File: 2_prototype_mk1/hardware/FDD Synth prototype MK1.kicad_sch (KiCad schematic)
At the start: 4 parts, among them U1 74AHCT245d

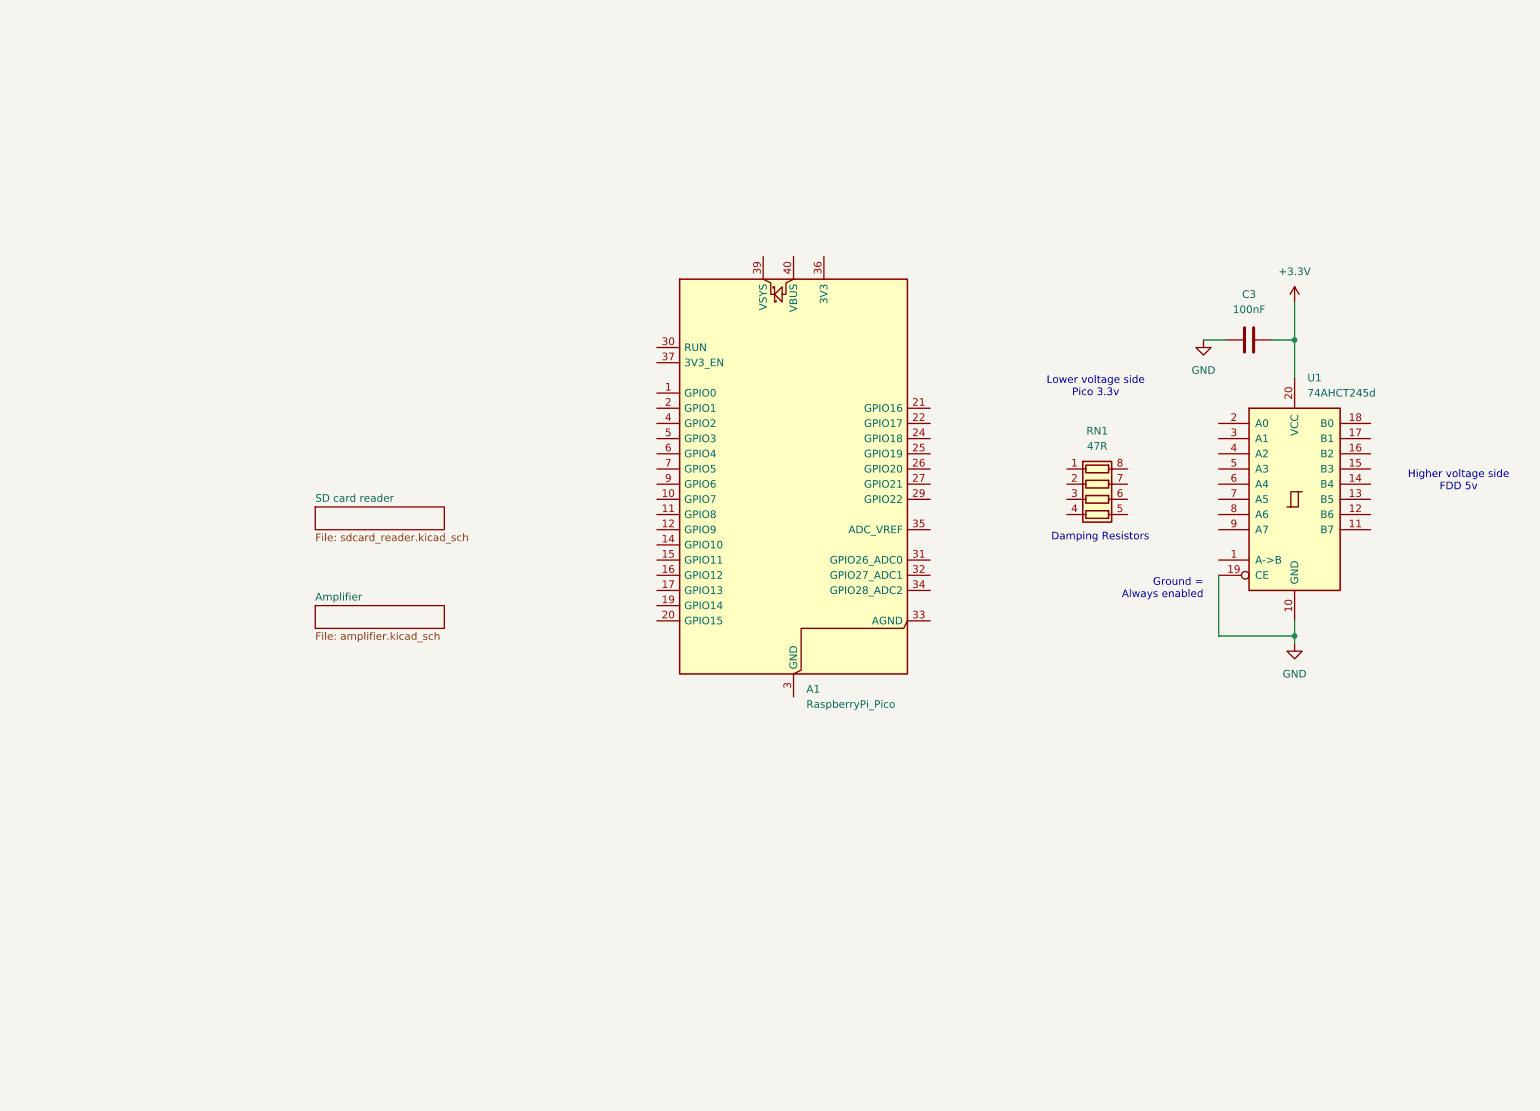
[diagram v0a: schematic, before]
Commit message: Created basic PCB
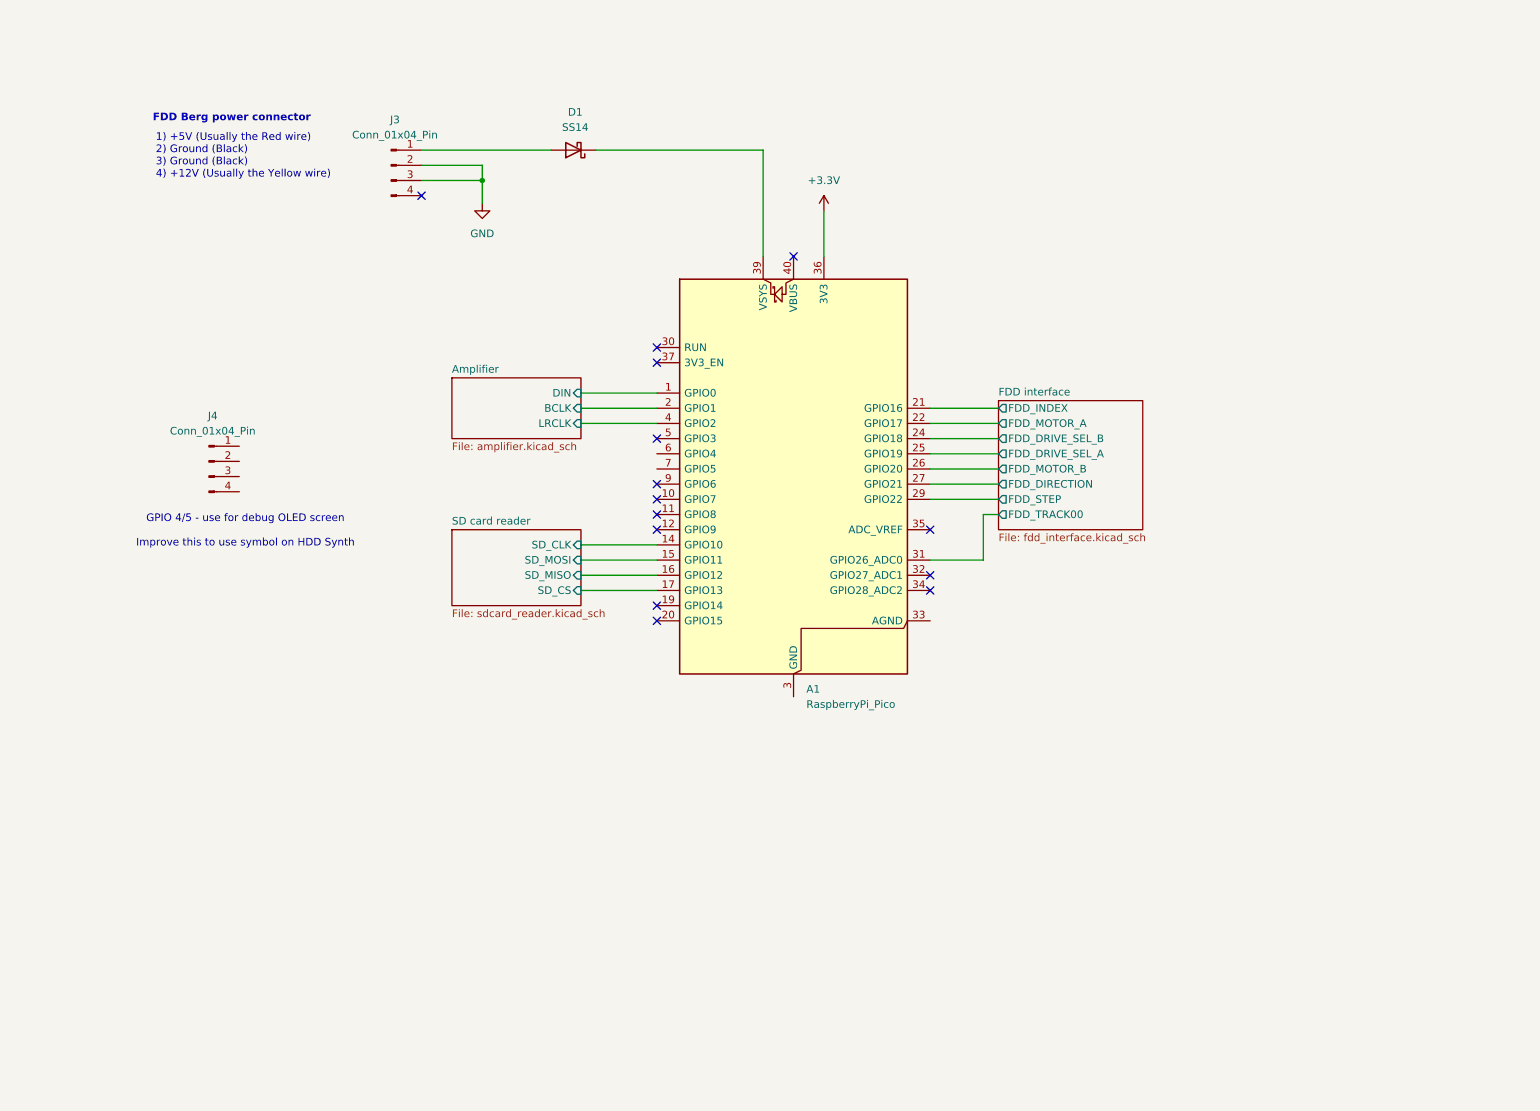
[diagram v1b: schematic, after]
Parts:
- removed C3: 100nF, Capacitor_SMD:C_0603_1608Metric, symbol Device:C
- removed RN1: 47R, Resistor_SMD:R_Array_Convex_4x0603, symbol Device:R_Pack04
- removed U1: 74AHCT245d, Package_SO:SOIC-20W_7.5x12.8mm_P1.27mm, symbol 74xx:74LS245
- added D1: SS14, Diode_SMD:D_SMA, symbol Device:D_Schottky
- added J3: Conn_01x04_Pin, Connector_JST:JST_XH_B4B-XH-A_1x04_P2.50mm_Vertical, symbol Connector:Conn_01x04_Pin
- added J4: Conn_01x04_Pin, Connector_PinSocket_2.54mm:PinSocket_1x04_P2.54mm_Vertical, symbol Connector:Conn_01x04_Pin
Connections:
- net +3.3V: now also A1.36 (3V3)
- net GND: now also J3.2 (Pin_2), J3.3 (Pin_3)
- net Amplifier/DIN: now reaches A1.1 (GPIO0)
- net SD card reader/SD_CLK: now reaches A1.14 (GPIO10)
- net SD card reader/SD_MOSI: now reaches A1.15 (GPIO11)
- net SD card reader/SD_MISO: now reaches A1.16 (GPIO12)
- net SD card reader/SD_CS: now reaches A1.17 (GPIO13)
- net Amplifier/BCLK: now reaches A1.2 (GPIO1)
- net FDD interface/FDD_INDEX: now reaches A1.21 (GPIO16)
- net FDD interface/FDD_MOTOR_A: now reaches A1.22 (GPIO17)
- net FDD interface/FDD_DRIVE_SEL_B: now reaches A1.24 (GPIO18)
- net FDD interface/FDD_DRIVE_SEL_A: now reaches A1.25 (GPIO19)
- net FDD interface/FDD_MOTOR_B: now reaches A1.26 (GPIO20)
- net FDD interface/FDD_DIRECTION: now reaches A1.27 (GPIO21)
- net FDD interface/FDD_STEP: now reaches A1.29 (GPIO22)
- net FDD interface/FDD_TRACK00: now reaches A1.31 (GPIO26_ADC0)
- net at A1.39 (VSYS): now also D1.1 (K)
- net Amplifier/LRCLK: now reaches A1.4 (GPIO2)
- new net: D1.2 (A), J3.1 (Pin_1)
- no-connect marks 0 -> 14
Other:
- added sheet FDD interface (fdd_interface.kicad_sch)
- sheet Amplifier ports: added BCLK, DIN, LRCLK; removed none
- sheet SD card reader ports: added SD_CLK, SD_CS, SD_MISO, SD_MOSI; removed none
- note added: "1) +5V (Usually the Red wire) 2) Ground (Black) 3) Ground (Black) 4) +12V (Usually the Yellow wire)"
- note added: "FDD Berg power connector"
- note added: "GPIO 4/5 - use for debug OLED screen Improve this to use symbol on HDD Synth"
- note removed: "Damping Resistors"
- note removed: "Ground = Always enabled"
- note removed: "Higher voltage side FDD 5v"
- note removed: "Lower voltage side Pico 3.3v"

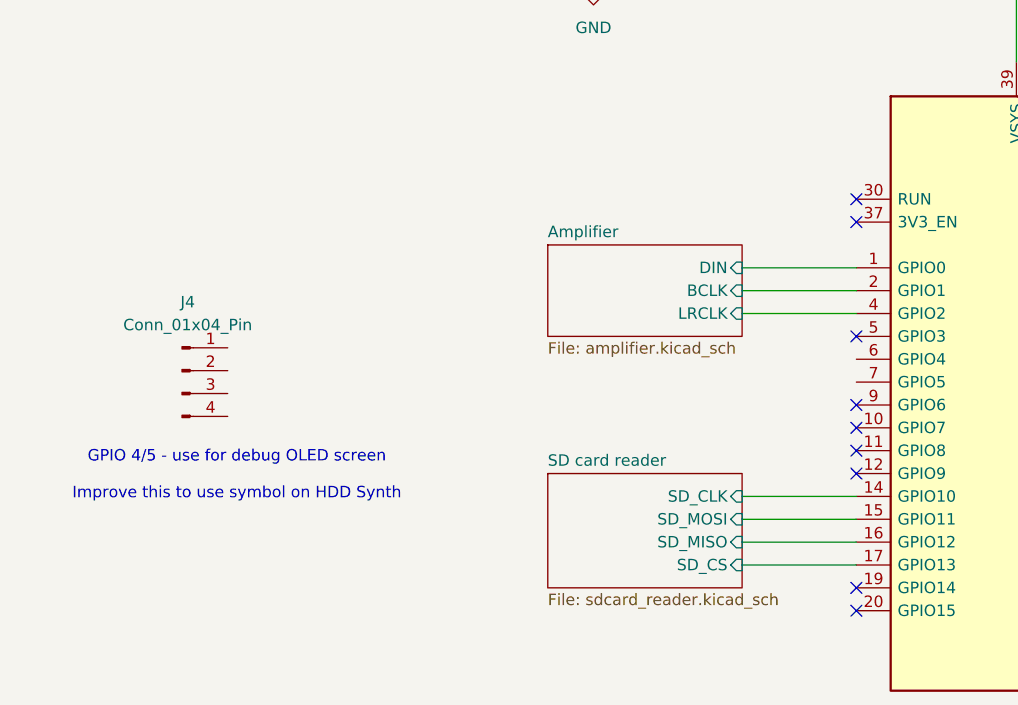
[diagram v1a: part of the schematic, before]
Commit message: Add OLED screen header
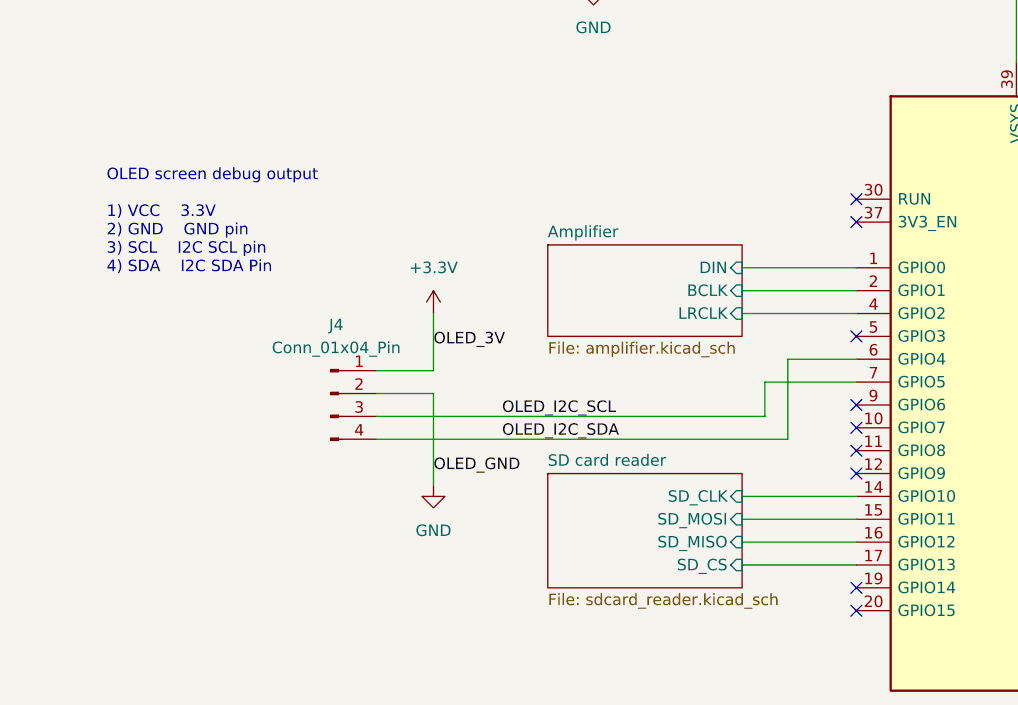
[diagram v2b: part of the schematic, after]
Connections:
- net +3.3V: now also J4.1 (Pin_1)
- net GND: now also J4.2 (Pin_2)
- net OLED_I2C_SDA: now reaches A1.6 (GPIO4)
- net OLED_I2C_SDA: now also J4.4 (Pin_4)
- net OLED_I2C_SCL: now reaches A1.7 (GPIO5)
- net OLED_I2C_SCL: now also J4.3 (Pin_3)
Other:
- note added: "OLED screen debug output 1) VCC 3.3V 2) GND GND pin 3) SCL I2C SCL pin 4) SDA I2C SDA Pin"
- note removed: "GPIO 4/5 - use for debug OLED screen Improve this to use symbol on HDD Synth"
- moved on the sheet: J4

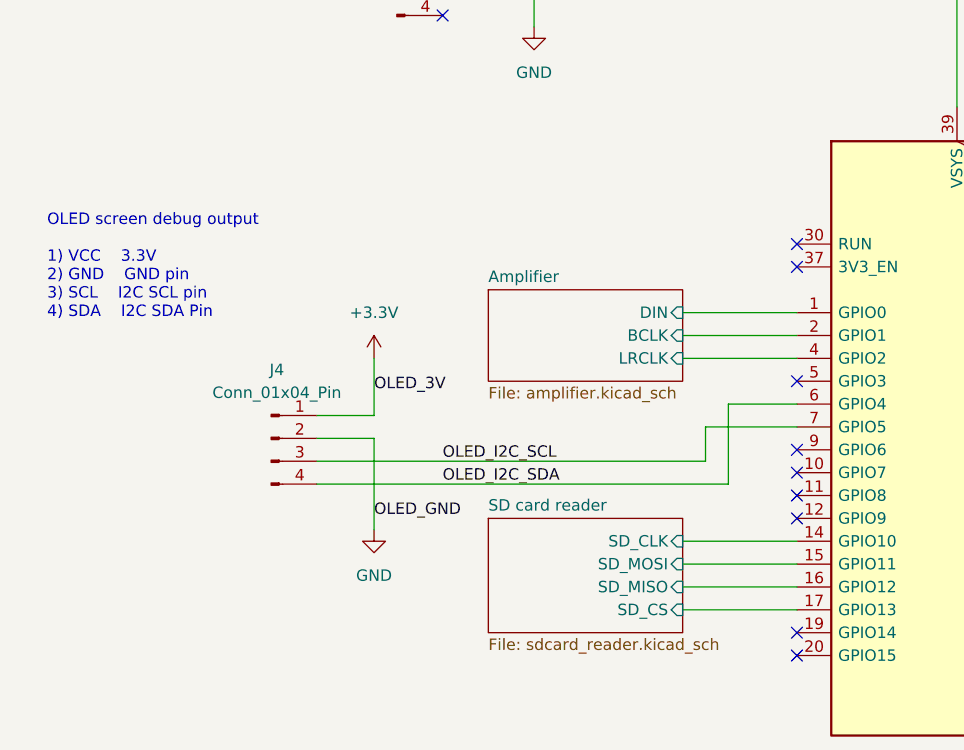
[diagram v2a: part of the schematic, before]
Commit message: Create LED and OLED connections
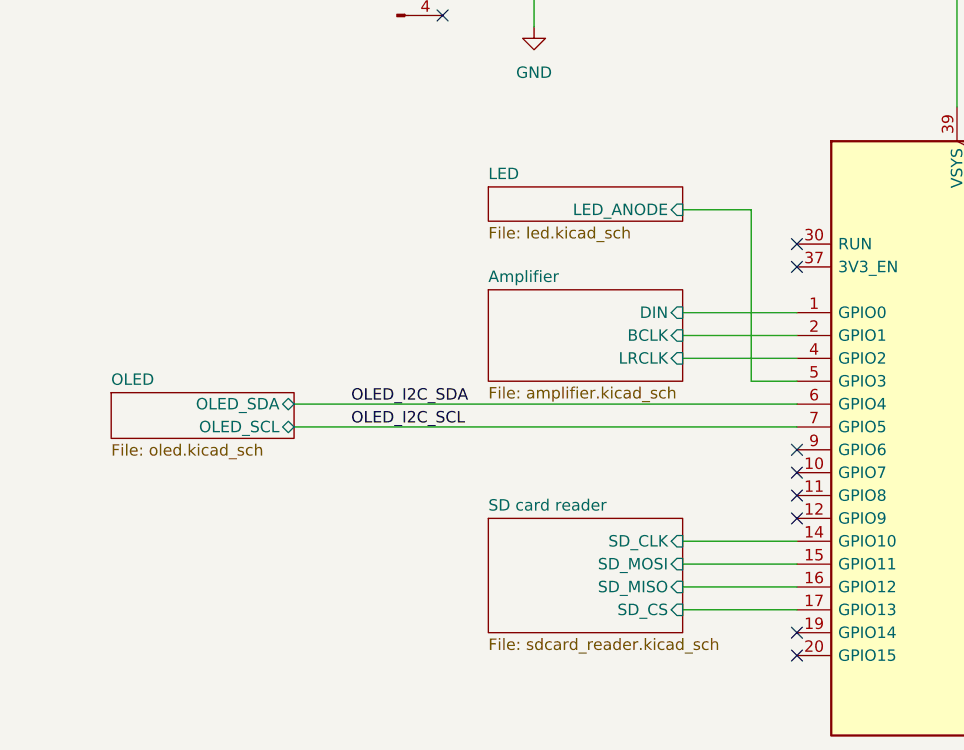
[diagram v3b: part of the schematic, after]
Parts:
- removed J4: Conn_01x04_Pin, Connector_PinSocket_2.54mm:PinSocket_1x04_P2.54mm_Vertical, symbol Connector:Conn_01x04_Pin
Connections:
- net LED/LED_ANODE: now reaches A1.5 (GPIO3)
- no-connect marks 14 -> 13
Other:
- added sheet LED (led.kicad_sch)
- added sheet OLED (oled.kicad_sch)
- note removed: "OLED screen debug output 1) VCC 3.3V 2) GND GND pin 3) SCL I2C SCL pin 4) SDA I2C SDA Pin"
